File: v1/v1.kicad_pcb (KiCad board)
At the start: 2 copper layers, 101.5 x 105.4 mm, 59 parts, among them CON1 SNES-CONN

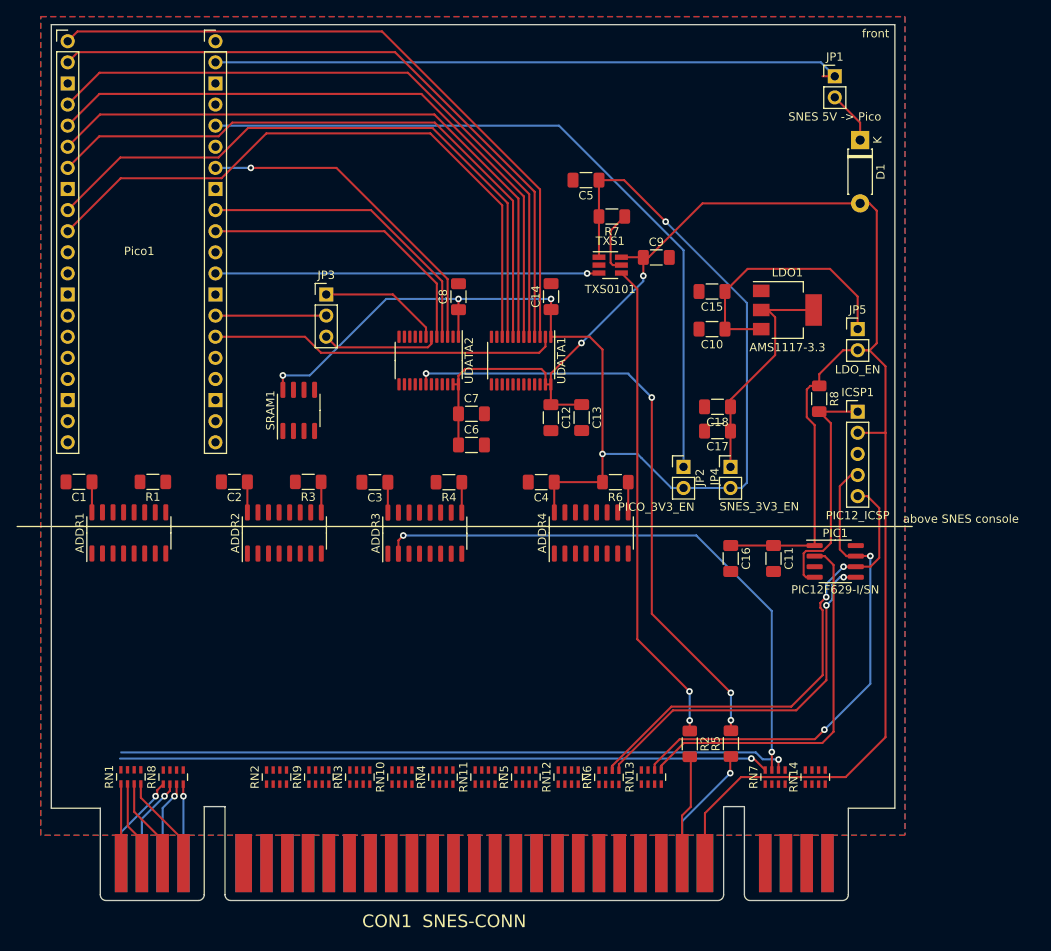
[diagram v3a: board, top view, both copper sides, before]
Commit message: v1: lots of routing and better placement of components
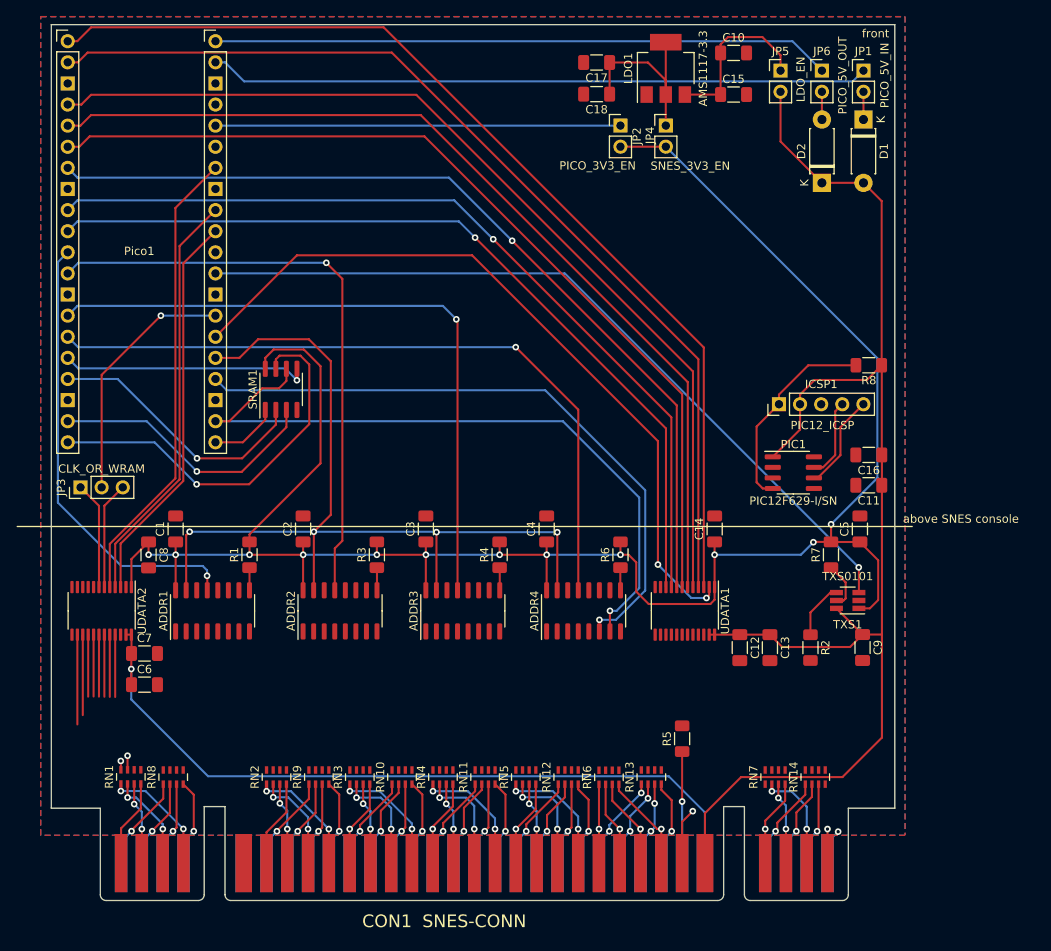
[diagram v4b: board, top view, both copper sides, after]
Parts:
- added D2: 1N5818, Diode_THT:D_DO-41_SOD81_P7.62mm_Horizontal, F.Cu at (179.0, 47.5)
- added JP6: PICO_5V_OUT, Connector_PinHeader_2.54mm:PinHeader_1x02_P2.54mm_Vertical, F.Cu at (179.0, 34.0)
- JP1: value SNES 5V -> Pico -> PICO_5V_IN
- moved C5 53.4 mm to (183.6, 89.1), turned to 90 degrees
- moved C9 53.1 mm to (183.9, 103.4), turned to -90 degrees
- moved UDATA2 49.6 mm to (92.3, 99.0)
- moved TXS1 49.4 mm to (182.1, 97.8), turned to 180 degrees
- moved C6 48.8 mm to (97.5, 107.9)
- moved C7 48.8 mm to (97.5, 104.1)
- moved C8 48.5 mm to (98.0, 92.3), turned to -90 degrees
- moved R7 48.5 mm to (180.1, 92.2), turned to 90 degrees
- moved C17 46.7 mm to (151.9, 33.0)
- moved JP4 41.8 mm to (160.2, 40.6)
- moved JP2 41.8 mm to (154.8, 40.6)
- moved C18 40.3 mm to (151.9, 36.8)
- moved JP3 37.6 mm to (89.8, 84.1), turned to 90 degrees
- moved UDATA1 36.0 mm to (162.5, 99.0)
- moved C12 35.8 mm to (169.1, 103.4)
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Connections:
- Pico1 pad 40: unconnected-(Pico1-Pad40) -> Net-(JP6-Pad1)
- RN1 pad 1: /XCLK_21.477MHZ -> /X~{PARD}
- RN1 pad 2: /XEXPAND -> /XPA6
- RN1 pad 3: /XPA6 -> /XEXPAND
- RN1 pad 4: /X~{PARD} -> /XCLK_21.477MHZ
- RN1 pad 5: /Y~{PARD} -> /YCLK_21.477MHZ
- RN1 pad 6: /YPA6 -> /YEXPAND
- RN1 pad 7: /YEXPAND -> /YPA6
- RN1 pad 8: /YCLK_21.477MHZ -> /Y~{PARD}
- RN2 pad 1: /XA11 -> /XA8
- RN2 pad 2: /XA10 -> /XA9
- RN2 pad 3: /XA9 -> /XA10
- RN2 pad 4: /XA8 -> /XA11
- RN2 pad 5: /YA8 -> /YA11
- RN2 pad 6: /YA9 -> /YA10
- RN2 pad 7: /YA10 -> /YA9
- RN2 pad 8: /YA11 -> /YA8
- RN3 pad 1: /XA7 -> /XA4
- RN3 pad 2: /XA6 -> /XA5
- RN3 pad 3: /XA5 -> /XA6
- RN3 pad 4: /XA4 -> /XA7
- RN3 pad 5: /YA4 -> /YA7
- RN3 pad 6: /YA5 -> /YA6
- RN3 pad 7: /YA6 -> /YA5
- RN3 pad 8: /YA7 -> /YA4
- RN4 pad 1: /XA3 -> /XA0
- RN4 pad 2: /XA2 -> /XA1
- RN4 pad 3: /XA1 -> /XA2
- RN4 pad 4: /XA0 -> /XA3
- RN4 pad 5: /YA0 -> /YA3
- RN4 pad 6: /YA1 -> /YA2
- RN4 pad 7: /YA2 -> /YA1
- RN4 pad 8: /YA3 -> /YA0
- RN5 pad 1: /X~{IRQ} -> /XD2
- RN5 pad 2: /XD0 -> /XD1
- RN5 pad 3: /XD1 -> /XD0
- RN5 pad 4: /XD2 -> /X~{IRQ}
- RN5 pad 5: /YD2 -> /Y~{IRQ}
- RN5 pad 6: /YD1 -> /YD0
- RN5 pad 7: /YD0 -> /YD1
- RN5 pad 8: /Y~{IRQ} -> /YD2
- RN7 pad 1: /XPA0 -> unconnected-(RN7-Pad1)
- RN7 pad 2: /XPA2 -> /XPA4
- RN7 pad 3: /XPA4 -> /XPA2
- RN7 pad 4: unconnected-(RN7-Pad4) -> /XPA0
- RN7 pad 5: unconnected-(RN7-Pad5) -> /YPA0
- RN7 pad 6: /YPA4 -> /YPA2
- RN7 pad 7: /YPA2 -> /YPA4
- RN7 pad 8: /YPA0 -> unconnected-(RN7-Pad8)
- UDATA2 pad 19: /Y~{RD} -> /Y~{CE}
- UDATA2 pad 21: /Y~{CE} -> /Y~{RD}
- UDATA2 pad 3: /~{CE} -> /~{RD}
- UDATA2 pad 5: /~{RD} -> /~{CE}
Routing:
- net /~{ADDRLD}: track 0.00 -> 109.8 mm, vias 0 -> 4
- net /ADDR4QH: track 0.00 -> 86.8 mm, vias 0 -> 1
- net /CLK_133MHZ: track 0.00 -> 84.8 mm, vias 0 -> 1
- net +3.3V: track 164.4 -> 245.6 mm, vias 5 -> 12
- net /YPA4: track 80.7 -> 0.00 mm, vias 1 -> 0
- net /ADDR3QH: track 0.00 -> 80.6 mm, vias 0 -> 1
- net /YPA0: track 78.2 -> 0.00 mm, vias 1 -> 0
- net /CLK_INH: track 0.00 -> 77.7 mm, vias 0 -> 1
- net Net-(JP6-Pad1): track 0.00 -> 74.4 mm
- net /ADDR2QH: track 0.00 -> 72.2 mm, vias 0 -> 1
- net /YPA2: track 69.7 -> 0.00 mm, vias 2 -> 0
- net /YCPU_CLK: track 73.6 -> 7.46 mm, vias 4 -> 0
- net /ADDR1QH: track 0.00 -> 54.4 mm, vias 0 -> 1
- net /Y~{RESET}: track 58.5 -> 6.80 mm, vias 2 -> 0
- net /CIC_IN: track 60.4 -> 9.65 mm, vias 2 -> 0
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
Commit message: v1: cleaned up more routing
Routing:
- net /CLK_133MHZ: track 84.8 -> 138.2 mm, vias 1 -> 7
- net /CLK_INH: track 77.7 -> 129.4 mm
- net /YA12: track 0.00 -> 1.39 mm, vias 0 -> 1
- net /YA8: track 0.00 -> 1.39 mm, vias 0 -> 1
- net /YA16: track 0.00 -> 1.38 mm, vias 0 -> 1
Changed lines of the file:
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@@
   (segment (start 179.67414 129.34962) (end 179.67414 126.846887) (width 0.25) (layer "B.Cu") (net 60))
   (segment (start 179.67414 126.846887) (end 180.953669 125.567358) (width 0.25) (layer "B.Cu") (net 60))
+  (segment (start 138.559902 99.3755) (end 137.695 100.240402) (width 0.25) (layer "F.Cu") (net 64))
+  (segment (start 122.065 99.365) (end 108.569695 99.365) (width 0.25) (layer "F.Cu") (net 64))
+  (segment (start 152.23 100.08) (end 151.5255 99.3755) (width 0.25) (layer "F.Cu") (net 64))
+  (segment (start 137.695 100.240402) (end 136.830098 99.3755) (width 0.25) (layer "F.Cu") (net 64))
+  (segment (start 122.925 100.155) (end 122.925 101.475) (width 0.25) (layer "F.Cu") (net 64))
+  (segment (start 137.695 100.240402) (end 137.695 101.475) (width 0.25) (layer "F.Cu") (net 64))
+  (segment (start 123.7045 99.3755) (end 122.925 100.155) (width 0.25) (layer "F.Cu") (net 64))
+  (segment (start 108.569695 99.365) (end 107.585 100.349695) (width 0.25) (layer "F.Cu") (net 64))
+  (segment locked (start 151.5255 99.3755) (end 138.559902 99.3755) (width 0.25) (layer "F.Cu") (net 64))
+  (segment (start 122.925 101.475) (end 122.925 100.225) (width 0.25) (layer "F.Cu") (net 64))
   (segment (start 152.225 101.475) (end 152.225 100.085) (width 0.25) (layer "F.Cu") (net 64))
+  (segment (start 107.585 100.349695) (end 107.585 101.475) (width 0.25) (layer "F.Cu") (net 64))
+  (segment locked (start 136.830098 99.3755) (end 123.7045 99.3755) (width 0.25) (layer "F.Cu") (net 64))
   (segment (start 152.225 100.085) (end 152.23 100.08) (width 0.25) (layer "F.Cu") (net 64))
+  (segment (start 122.925 100.225) (end 122.065 99.365) (width 0.25) (layer "F.Cu") (net 64))
   (via (at 152.23 100.08) (size 0.8) (drill 0.4) (layers "F.Cu" "B.Cu") (net 64))
   (segment (start 106.03 71.1) (end 107.39 72.46) (width 0.25) (layer "B.Cu") (net 64))
@@
   (segment (start 145.71 72.46) (end 157.74 84.49) (width 0.25) (layer "B.Cu") (net 64))
   (segment (start 110.125 96.525) (end 110.125 93.8) (width 0.25) (layer "F.Cu") (net 65))
-  (segment (start 105.045 96.525) (end 105.045 94.805) (width 0.25) (layer "F.Cu") (net 78))
-  (segment (start 105.045 94.805) (end 105.02 94.78) (width 0.25) (layer "F.Cu") (net 78))
-  (via (at 105.02 94.78) (size 0.8) (drill 0.4) (layers "F.Cu" "B.Cu") (net 78))
+  (segment (start 108.855 96.525) (end 108.855 95.145) (width 0.25) (layer "F.Cu") (net 66))
+  (segment (start 108.855 95.145) (end 108.86 95.14) (width 0.25) (layer "F.Cu") (net 66))
+  (via (at 108.86 95.14) (size 0.8) (drill 0.4) (layers "F.Cu" "B.Cu") (net 66))
+  (segment (start 105.045 95.145) (end 105.04 95.14) (width 0.25) (layer "F.Cu") (net 78))
+  (segment (start 105.045 96.525) (end 105.045 95.145) (width 0.25) (layer "F.Cu") (net 78))
+  (via (at 105.04 95.14) (size 0.8) (drill 0.4) (layers "F.Cu" "B.Cu") (net 78))
+  (segment (start 105.04 94.54) (end 105.04 95.14) (width 0.25) (layer "B.Cu") (net 78))
+  (segment (start 88.25 55.86) (end 87.07 57.04) (width 0.25) (layer "B.Cu") (net 78))
+  (segment (start 87.07 85.97) (end 94.93 93.83) (width 0.25) (layer "B.Cu") (net 78))
+  (segment (start 104.33 93.83) (end 105.04 94.54) (width 0.25) (layer "B.Cu") (net 78))
   (segment (start 87.07 57.04) (end 87.07 85.97) (width 0.25) (layer "B.Cu") (net 78))
-  (segment (start 105.04 94.8) (end 105.02 94.78) (width 0.25) (layer "B.Cu") (net 78))
-  (segment (start 88.25 55.86) (end 87.07 57.04) (width 0.25) (layer "B.Cu") (net 78))
-  (segment (start 94.7 93.6) (end 104.5 93.6) (width 0.25) (layer "B.Cu") (net 78))
-  (segment (start 87.07 85.97) (end 94.7 93.6) (width 0.25) (layer "B.Cu") (net 78))
-  (segment (start 104.5 93.6) (end 105.02 94.12) (width 0.25) (layer "B.Cu") (net 78))
-  (segment (start 105.02 94.12) (end 105.02 94.78) (width 0.25) (layer "B.Cu") (net 78))
+  (segment (start 94.93 93.83) (end 104.33 93.83) (width 0.25) (layer "B.Cu") (net 78))
+  (segment (start 107.585 95.145) (end 107.59 95.14) (width 0.25) (layer "F.Cu") (net 79))
+  (segment (start 107.585 96.525) (end 107.585 95.145) (width 0.25) (layer "F.Cu") (net 79))
+  (via (at 107.59 95.14) (size 0.8) (drill 0.4) (layers "F.Cu" "B.Cu") (net 79))
+  (segment (start 106.315 95.155) (end 106.32 95.15) (width 0.25) (layer "F.Cu") (net 83))
+  (segment (start 106.315 96.525) (end 106.315 95.155) (width 0.25) (layer "F.Cu") (net 83))
+  (via (at 106.32 95.15) (size 0.8) (drill 0.4) (layers "F.Cu" "B.Cu") (net 83))
   (segment (start 92.665 101.8625) (end 92.665 109.33793) (width 0.25) (layer "F.Cu") (net 91))
   (segment (start 90.715 101.8625) (end 90.715 109.321623) (width 0.25) (layer "F.Cu") (net 98))
@@
   (segment (start 133.395 62.305) (end 135.01 63.92) (width 0.25) (layer "B.Cu") (net 124))
   (segment (start 88.25 63.48) (end 89.425 62.305) (width 0.25) (layer "B.Cu") (net 124))
+  (segment locked (start 124.2 98.6455) (end 108.8655 98.6455) (width 0.25) (layer "F.Cu") (net 125))
   (segment (start 114.565 71.335) (end 114.565 69.875) (width 0.25) (layer "F.Cu") (net 125))
-  (segment (start 153.495 101.475) (end 153.495 99.005) (width 0.25) (layer "F.Cu") (net 125))
+  (segment locked (start 138.9755 98.6455) (end 124.2 98.6455) (width 0.25) (layer "F.Cu") (net 125))
+  (segment locked (start 138.98 98.65) (end 153.46 98.65) (width 0.25) (layer "F.Cu") (net 125))
+  (segment (start 108.8655 98.6455) (end 108.86 98.64) (width 0.25) (layer "F.Cu") (net 125))
+  (segment (start 153.495 101.475) (end 153.495 98.655) (width 0.25) (layer "F.Cu") (net 125))
+  (segment (start 138.98 98.65) (end 138.9755 98.6455) (width 0.25) (layer "F.Cu") (net 125))
+  (segment (start 108.86 101.47) (end 108.855 101.475) (width 0.25) (layer "F.Cu") (net 125))
   (segment (start 106.03 76.18) (end 107.7 76.18) (width 0.25) (layer "F.Cu") (net 125))
   (segment (start 111.66 72.22) (end 113.68 72.22) (width 0.25) (layer "F.Cu") (net 125))
+  (segment (start 138.965 101.475) (end 138.965 100.105) (width 0.25) (layer "F.Cu") (net 125))
+  (segment (start 124.195 101.475) (end 124.195 100.105) (width 0.25) (layer "F.Cu") (net 125))
+  (segment (start 124.195 100.105) (end 124.2 100.1) (width 0.25) (layer "F.Cu") (net 125))
   (segment (start 107.7 76.18) (end 111.66 72.22) (width 0.25) (layer "F.Cu") (net 125))
   (segment (start 113.68 72.22) (end 114.565 71.335) (width 0.25) (layer "F.Cu") (net 125))
-  (segment (start 153.495 99.005) (end 153.5 99) (width 0.25) (layer "F.Cu") (net 125))
-  (via (at 153.5 99) (size 0.8) (drill 0.4) (layers "F.Cu" "B.Cu") (net 125))
-  (segment (start 154.29 99) (end 157.02 96.27) (width 0.25) (layer "B.Cu") (net 125))
-  (segment (start 153.5 99) (end 154.29 99) (width 0.25) (layer "B.Cu") (net 125))
-  (segment (start 147.82569 76.18) (end 106.03 76.18) (width 0.25) (layer "B.Cu") (net 125))
-  (segment (start 157.02 85.37431) (end 147.82569 76.18) (width 0.25) (layer "B.Cu") (net 125))
-  (segment (start 157.02 96.27) (end 157.02 85.37431) (width 0.25) (layer "B.Cu") (net 125))
+  (segment (start 108.86 100.1) (end 108.86 101.47) (width 0.25) (layer "F.Cu") (net 125))
+  (segment (start 138.965 100.105) (end 138.97 100.1) (width 0.25) (layer "F.Cu") (net 125))
+  (segment (start 153.495 98.655) (end 153.49 98.65) (width 0.25) (layer "F.Cu") (net 125))
+  (via (at 153.49 98.65) (size 0.8) (drill 0.4) (layers "F.Cu" "B.Cu") (net 125))
+  (via (at 138.97 100.1) (size 0.8) (drill 0.4) (layers "F.Cu" "B.Cu") (net 125))
+  (via locked (at 108.86 100.1) (size 0.8) (drill 0.4) (layers "F.Cu" "B.Cu") (net 125))
+  (via locked (at 108.86 98.64) (size 0.8) (drill 0.4) (layers "F.Cu" "B.Cu") (net 125))
+  (via (at 124.2 100.1) (size 0.8) (drill 0.4) (layers "F.Cu" "B.Cu") (net 125))
+  (via (at 138.98 98.65) (size 0.8) (drill 0.4) (layers "F.Cu" "B.Cu") (net 125))
+  (via locked (at 124.2 98.6455) (size 0.8) (drill 0.4) (layers "F.Cu" "B.Cu") (net 125))
+  (segment (start 138.97 100.1) (end 138.97 98.66) (width 0.25) (layer "B.Cu") (net 125))
+  (segment (start 147.82569 76.18) (end 157.02 85.37431) (width 0.25) (layer "B.Cu") (net 125))
+  (segment (start 124.2 98.6455) (end 124.2 100.1) (width 0.25) (layer "B.Cu") (net 125))
+  (segment (start 157.02 96.36) (end 154.73 98.65) (width 0.25) (layer "B.Cu") (net 125))
+  (segment (start 138.97 98.66) (end 138.98 98.65) (width 0.25) (layer "B.Cu") (net 125))
+  (segment (start 108.86 98.64) (end 108.86 100.1) (width 0.25) (layer "B.Cu") (net 125))
+  (segment (start 154.73 98.65) (end 153.49 98.65) (width 0.25) (layer "B.Cu") (net 125))
+  (segment (start 106.03 76.18) (end 147.82569 76.18) (width 0.25) (layer "B.Cu") (net 125))
+  (segment (start 157.02 85.37431) (end 157.02 96.36) (width 0.25) (layer "B.Cu") (net 125))
   (segment (start 154.739585 93.820415) (end 154.739585 96.499585) (width 0.25) (layer "F.Cu") (net 126))
   (segment (start 154.739585 96.499585) (end 154.76 96.52) (width 0.25) (layer "F.Cu") (net 126))

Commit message: v1: more routing progress
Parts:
- moved TXS1 1.89 mm to (180.2, 97.7)
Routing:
- net /YPA0: track 0.00 -> 86.3 mm, vias 0 -> 2
- net /YPA4: track 0.00 -> 86.1 mm, vias 0 -> 2
- net /YCPU_CLK: track 7.46 -> 80.3 mm, vias 0 -> 2
- net /YPA5: track 0.00 -> 70.5 mm, vias 0 -> 2
- net /Y~{WR}: track 7.49 -> 77.5 mm, vias 0 -> 2
- net /YPA1: track 0.00 -> 69.9 mm, vias 0 -> 2
- net /CIC_CLK: track 0.00 -> 65.8 mm, vias 0 -> 2
- net /Y~{RD}: track 7.50 -> 72.3 mm, vias 0 -> 2
- net /CIC_OUT: track 11.1 -> 73.4 mm, vias 0 -> 2
- net /CIC_RST: track 0.00 -> 60.3 mm, vias 0 -> 2
- net /Y~{CE}: track 7.48 -> 67.5 mm, vias 0 -> 2
- net /CIC_IN: track 9.65 -> 68.6 mm, vias 0 -> 2
- net /Y~{IRQ}: track 7.46 -> 65.5 mm, vias 0 -> 2
- net /YPA7: track 0.00 -> 58.0 mm, vias 0 -> 2
- net /YPA2: track 0.00 -> 56.5 mm, vias 0 -> 2
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
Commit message: v1: completed routing
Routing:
- net /YA11: track 8.05 -> 56.8 mm, vias 2 -> 4
- net /YA15: track 2.67 -> 50.2 mm
- net /YA21: track 2.57 -> 47.5 mm
- net /YA0: track 0.00 -> 43.4 mm, vias 0 -> 2
- net /YA20: track 8.40 -> 50.3 mm, vias 3 -> 2
- net /YA7: track 0.00 -> 41.6 mm, vias 0 -> 2
- net /YA10: track 4.35 -> 45.5 mm, vias 2 -> 4
- net /CLK_133MHZ: track 138.2 -> 98.8 mm, vias 7 -> 2
- net /YA19: track 1.38 -> 40.2 mm, vias 1 -> 2
- net /YA14: track 2.59 -> 39.6 mm, vias 2 -> 4
- net /YA4: track 0.00 -> 29.7 mm, vias 0 -> 2
- net /YA1: track 0.00 -> 29.6 mm, vias 0 -> 2
- net /YA16: track 8.48 -> 38.0 mm, vias 3 -> 2
- net /YA13: track 2.55 -> 31.3 mm
- net /YA6: track 0.00 -> 28.4 mm, vias 0 -> 2
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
